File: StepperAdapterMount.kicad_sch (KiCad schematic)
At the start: 3 parts, among them M1 StepperMotor_4.7mm_Sanyo_ultr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

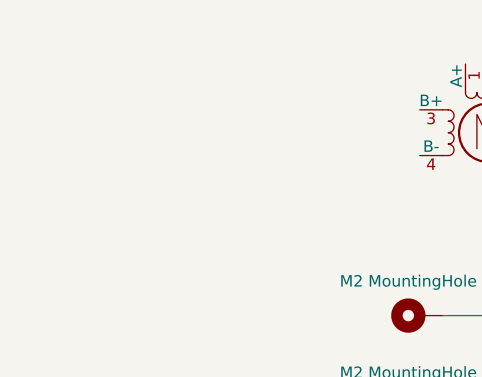
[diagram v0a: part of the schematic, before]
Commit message: Updated board shape
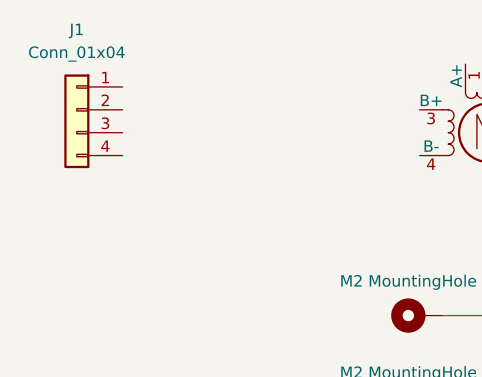
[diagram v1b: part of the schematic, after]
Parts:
- added J1: Conn_01x04, Connector_Molex:Molex_PicoBlade_53261-0471_1x04-1MP_P1.25mm_Horizontal, symbol Connector_Generic:Conn_01x04
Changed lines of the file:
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@@
+	)
+	(symbol
+		(lib_id "Connector_Generic:Conn_01x04")
+		(at 102.87 96.52 0)
+		(mirror y)
+		(unit 1)
+		(exclude_from_sim no)
+		(in_bom yes)
+		(on_board yes)
+		(dnp no)
+		(fields_autoplaced yes)
+		(property "Reference" "J1"
+			(at 102.87 87.63 0)
+			(effects
+				(font
+					(size 1.27 1.27)
+				)
+			)
+		)
+		(property "Value" "Conn_01x04"
+			(at 102.87 90.17 0)
+			(effects
+				(font
+					(size 1.27 1.27)
+				)
+			)
+		)
+		(property "Footprint" "Connector_Molex:Molex_PicoBlade_53261-0471_1x04-1MP_P1.25mm_Horizontal"
+			(at 102.87 96.52 0)
+			(effects
+				(font
+					(size 1.27 1.27)
+				)
+				(hide yes)
+			)
+		)
+		(property "Datasheet" "~"
+			(at 102.87 96.52 0)
+			(effects
+				(font
+					(size 1.27 1.27)
+				)
+				(hide yes)
+			)
+		)
+		(property "Description" "Generic connector, single row, 01x04, script generated (kicad-library-utils/schlib/autogen/connector/)"
+			(at 102.87 96.52 0)
+			(effects
+				(font
+					(size 1.27 1.27)
+				)
+				(hide yes)
+			)
+		)
+		(pin "4"
+		)
+		(pin "3"
+		)
+		(pin "2"
+		)
+		(pin "1"
+		)
+		(instances
+			(project ""
+				(path "/e7c24600-e1d4-4e1e-8b2a-6e1d00e73a4d"
+					(reference "J1")
+					(unit 1)
+				)
+			)
+		)
 	)
 	(symbol

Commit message: v1.0
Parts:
- removed H1, H2: M2 MountingHole, MountingHole:MountingHole_2.2mm_M2_ISO7380_Pad, symbol Mechanical:MountingHole_Pad
- added J2, J3, J4: Conn_01x04, Connector_PinHeader_2.54mm:PinHeader_1x04_P2.54mm_Vertical, symbol Connector_Generic:Conn_01x04
- added M2: StepperMotor_8mm_i500212644, AC-kicad-library:StepperMotor_8mm_i500212644, symbol AC-kicad-library:StepperMotor_8mm_i500212644
- J1: footprint Connector_Molex:Molex_PicoBlade_53261-0471_1x04-1MP_P1.25mm_Horizontal -> Connector_PinHeader_2.54mm:PinHeader_1x04_P2.54mm_Vertical
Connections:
- net A1+: now reaches M1.1 (A+)
- net A1+: now also J1.1 (Pin_1)
- net A1-: now reaches M1.2 (A-)
- net A1-: now also J2.1 (Pin_1)
- net B1+: now reaches M1.3 (B+)
- net B1+: now also J1.4 (Pin_4)
- net B1-: now reaches M1.4 (B-)
- net B1-: now also J2.4 (Pin_4)
- new net A2+: J3.1 (Pin_1), M2.1 (A+)
- new net A2-: J4.1 (Pin_1), M2.2 (A-)
- new net B2+: J3.4 (Pin_4), M2.3 (B+)
- new net B2-: J4.4 (Pin_4), M2.4 (B-)
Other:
- moved on the sheet: M1
